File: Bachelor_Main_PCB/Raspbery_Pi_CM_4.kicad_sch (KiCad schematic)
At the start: 4 parts, among them J21 M20-9990245, U1 SC0683, X1 DF40HC_3.0_-100DS-0.4V_58, X2 DF40HC_3.0_-100DS-0.4V_58

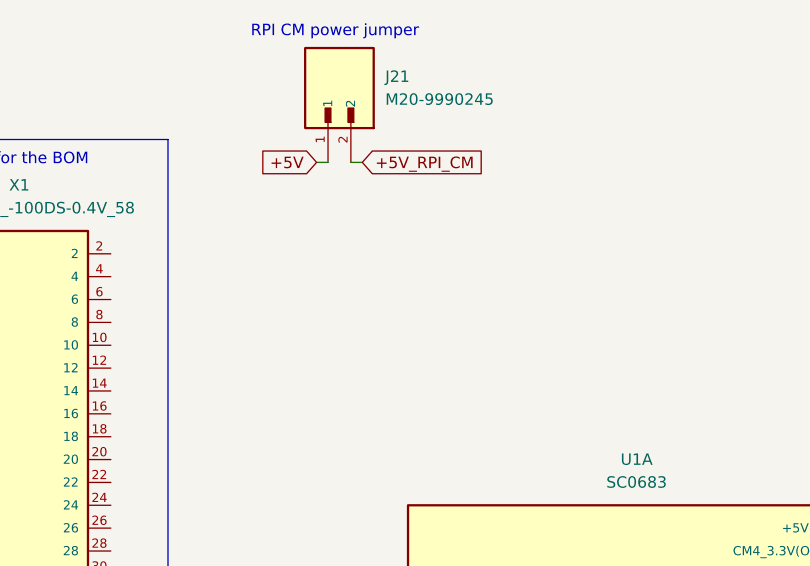
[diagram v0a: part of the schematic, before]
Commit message: Reinstated Mosfet RPI_CM_ENABLE controll
instead of enable pin on switch mode controller. this way the audiomoth can use the 5v supply with the capacitor multiplier.
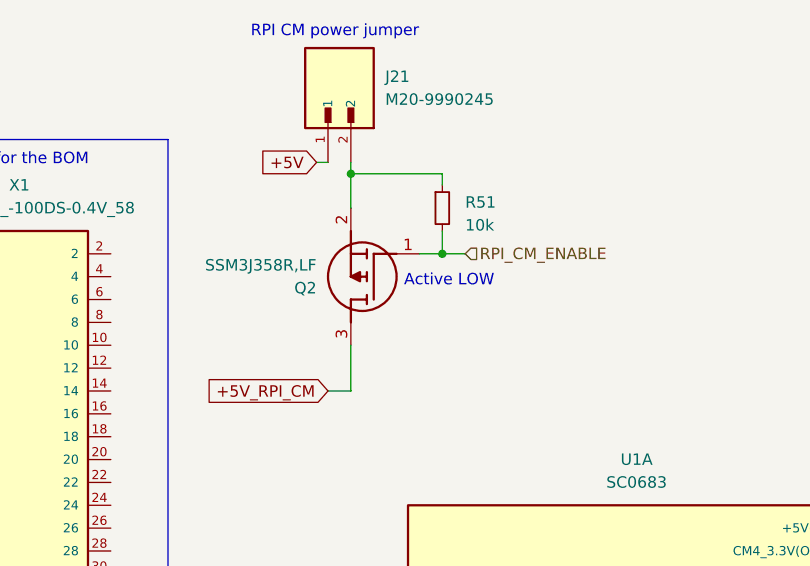
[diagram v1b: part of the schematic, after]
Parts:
- added Q2: SSM3J358R,LF, KiCad4:SOTFL95P240X88-3N, symbol SSM3J358R_LF:SSM3J358R,LF
- added R51: 10k, Resistor_SMD:R_0402_1005Metric, symbol Device:R_Small
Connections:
- net +5V_RPI_CM: now also Q2.3 (D); no longer J21.2
- new net: J21.2, Q2.2 (S), R51.1
- new net RPI_CM_ENABLE: Q2.1 (G), R51.2
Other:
- note added: "Active LOW"

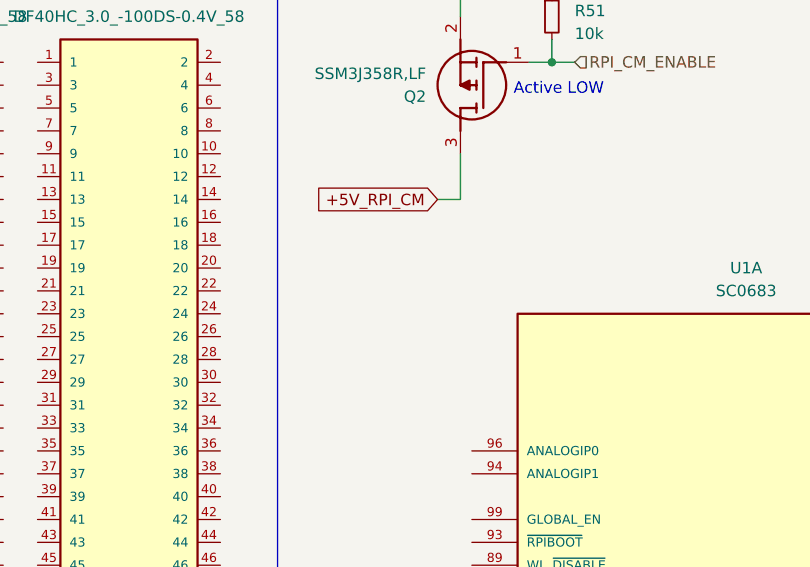
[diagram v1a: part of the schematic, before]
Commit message: Add green led to all power rails
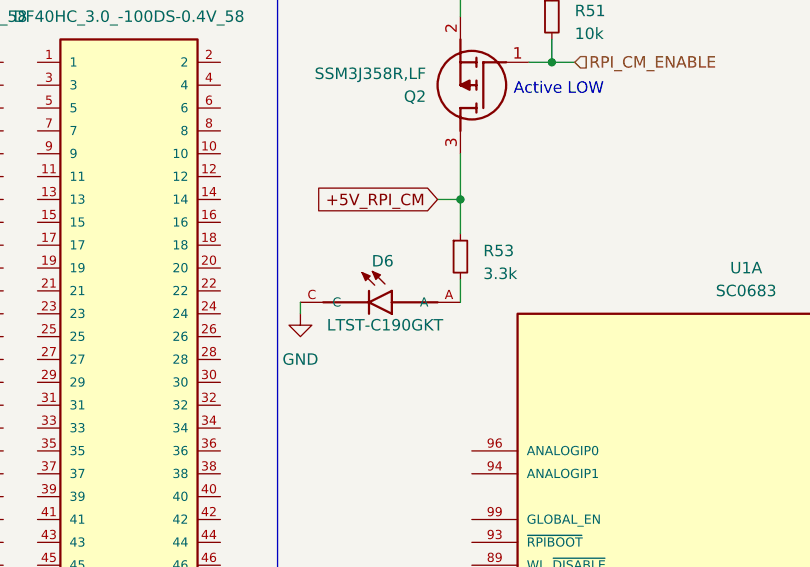
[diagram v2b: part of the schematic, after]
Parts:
- added D6: LTST-C190GKT, LTST-C190GKT:LEDM1608X80, symbol LTST-C190GKT:LTST-C190GKT
- added R53: 3.3k, Resistor_SMD:R_0402_1005Metric, symbol Device:R_Small
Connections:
- net +5V_RPI_CM: now also R53.1
- net GND: now also D6.C
- new net: D6.A, R53.2

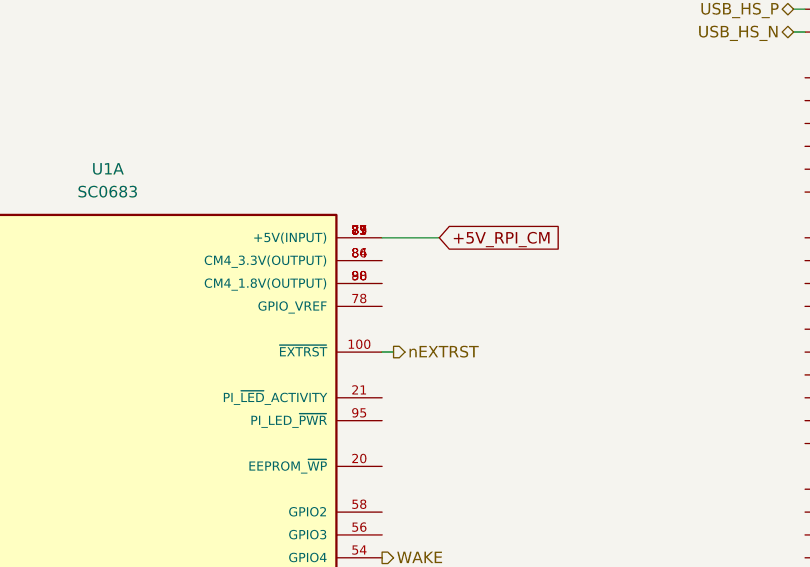
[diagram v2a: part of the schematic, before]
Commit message: connect RPI GPIO_VREF to internal 3,3v regulator
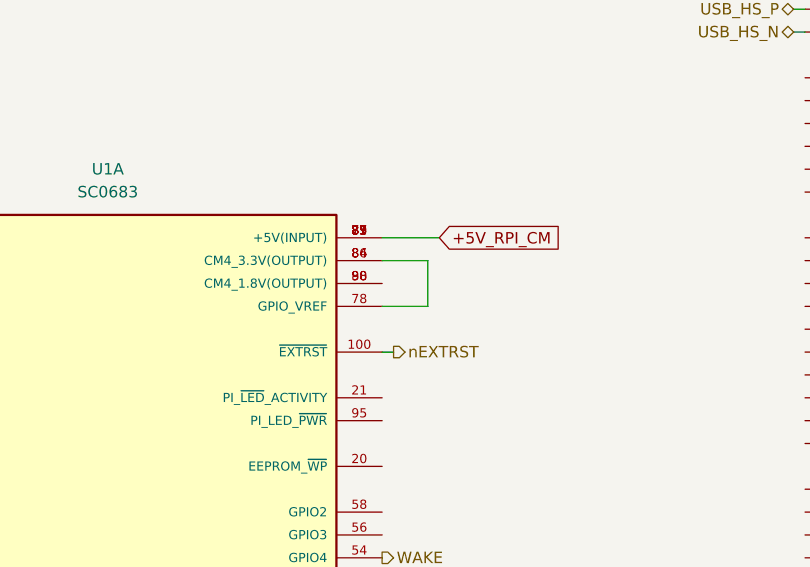
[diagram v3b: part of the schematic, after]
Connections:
- net at U1.78 (GPIO_VREF): now also U1.84 (CM4_3.3V(OUTPUT)), U1.86 (CM4_3.3V(OUTPUT))

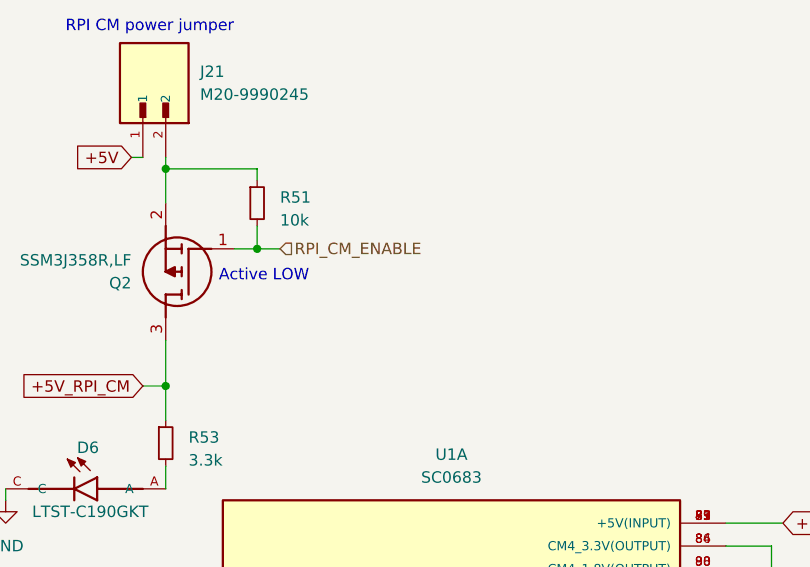
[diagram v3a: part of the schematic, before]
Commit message: Add signal inverter to RPIcm enable pin.
In order to protect MCU against 5v input on GPIO pin.
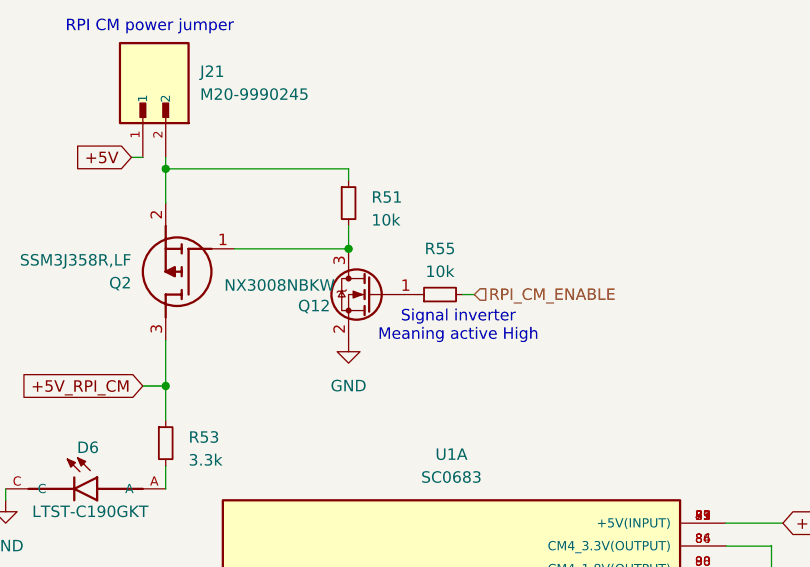
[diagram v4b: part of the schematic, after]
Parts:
- added Q12: NX3008NBKW, Package_TO_SOT_SMD:SOT-323_SC-70, symbol Device:Q_NMOS_GSD
- added R55: 10k, Resistor_SMD:R_0402_1005Metric, symbol Device:R_Small
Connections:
- net GND: now also Q12.2 (S)
- net RPI_CM_ENABLE: now also R55.2; no longer Q2.1 (G), R51.2
- new net: Q12.1 (G), R55.1
- new net: Q12.3 (D), Q2.1 (G), R51.2
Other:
- note added: "Signal inverter Meaning active High"
- note removed: "Active LOW"
- moved on the sheet: R51

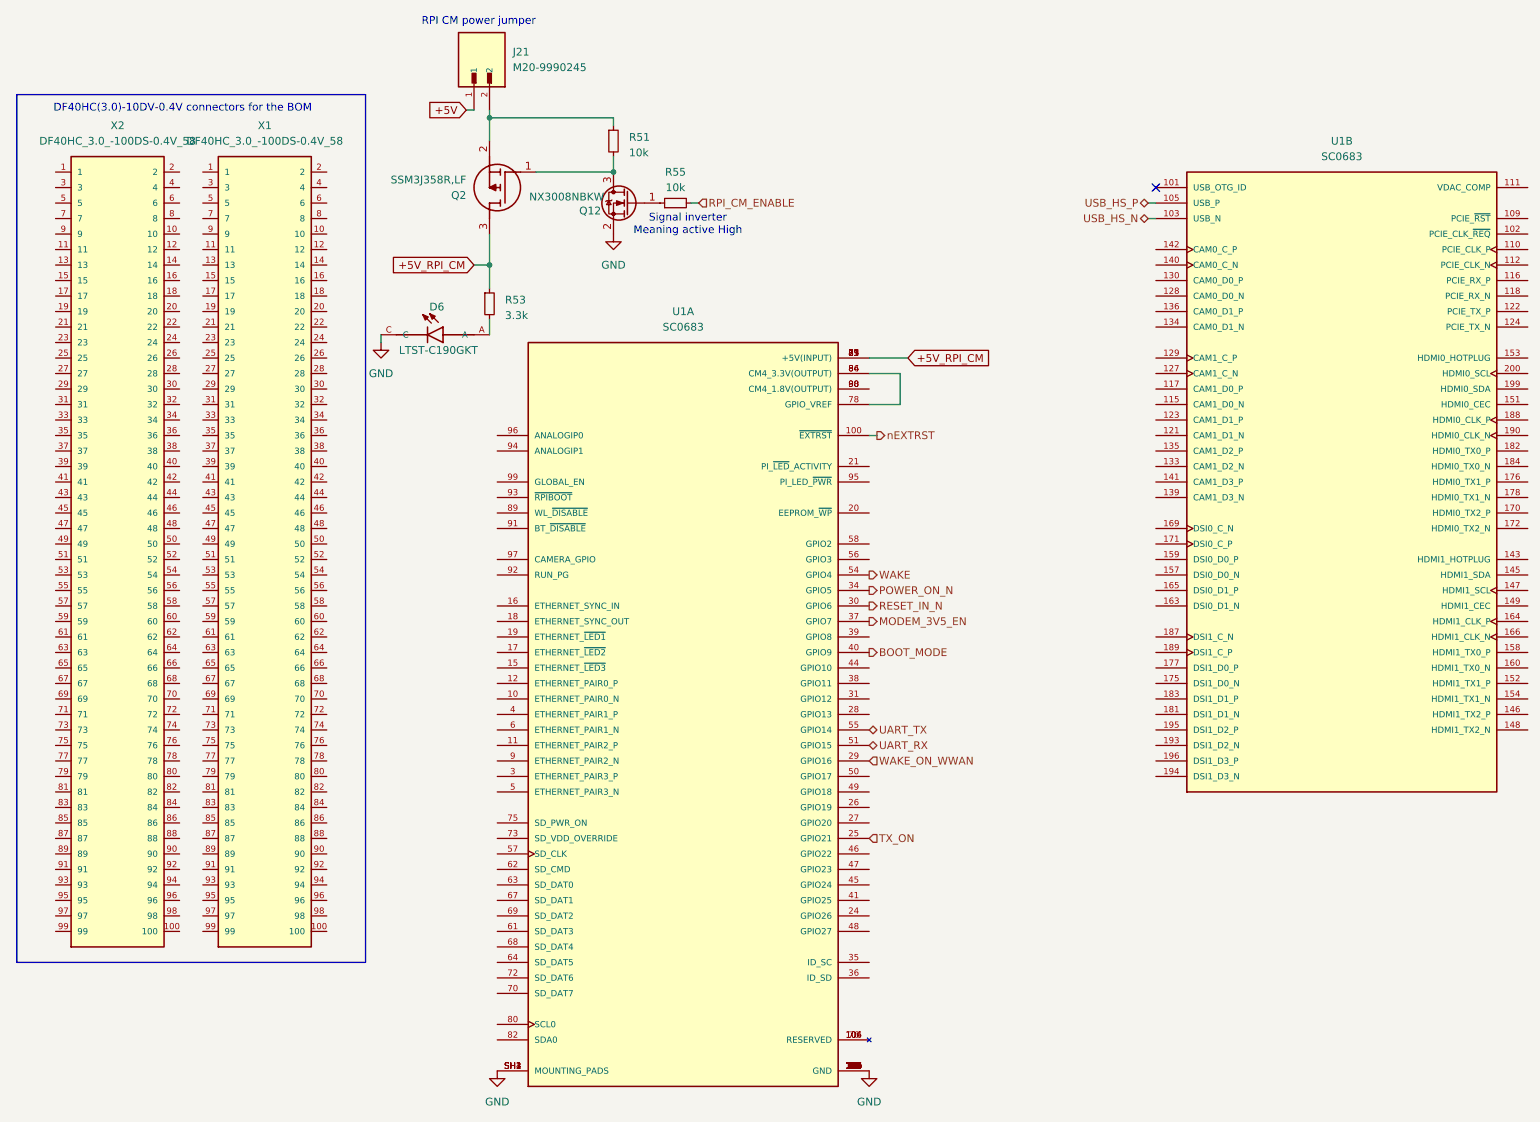
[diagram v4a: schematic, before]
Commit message: Updated the "Part-no" field in the symbol field table for all components
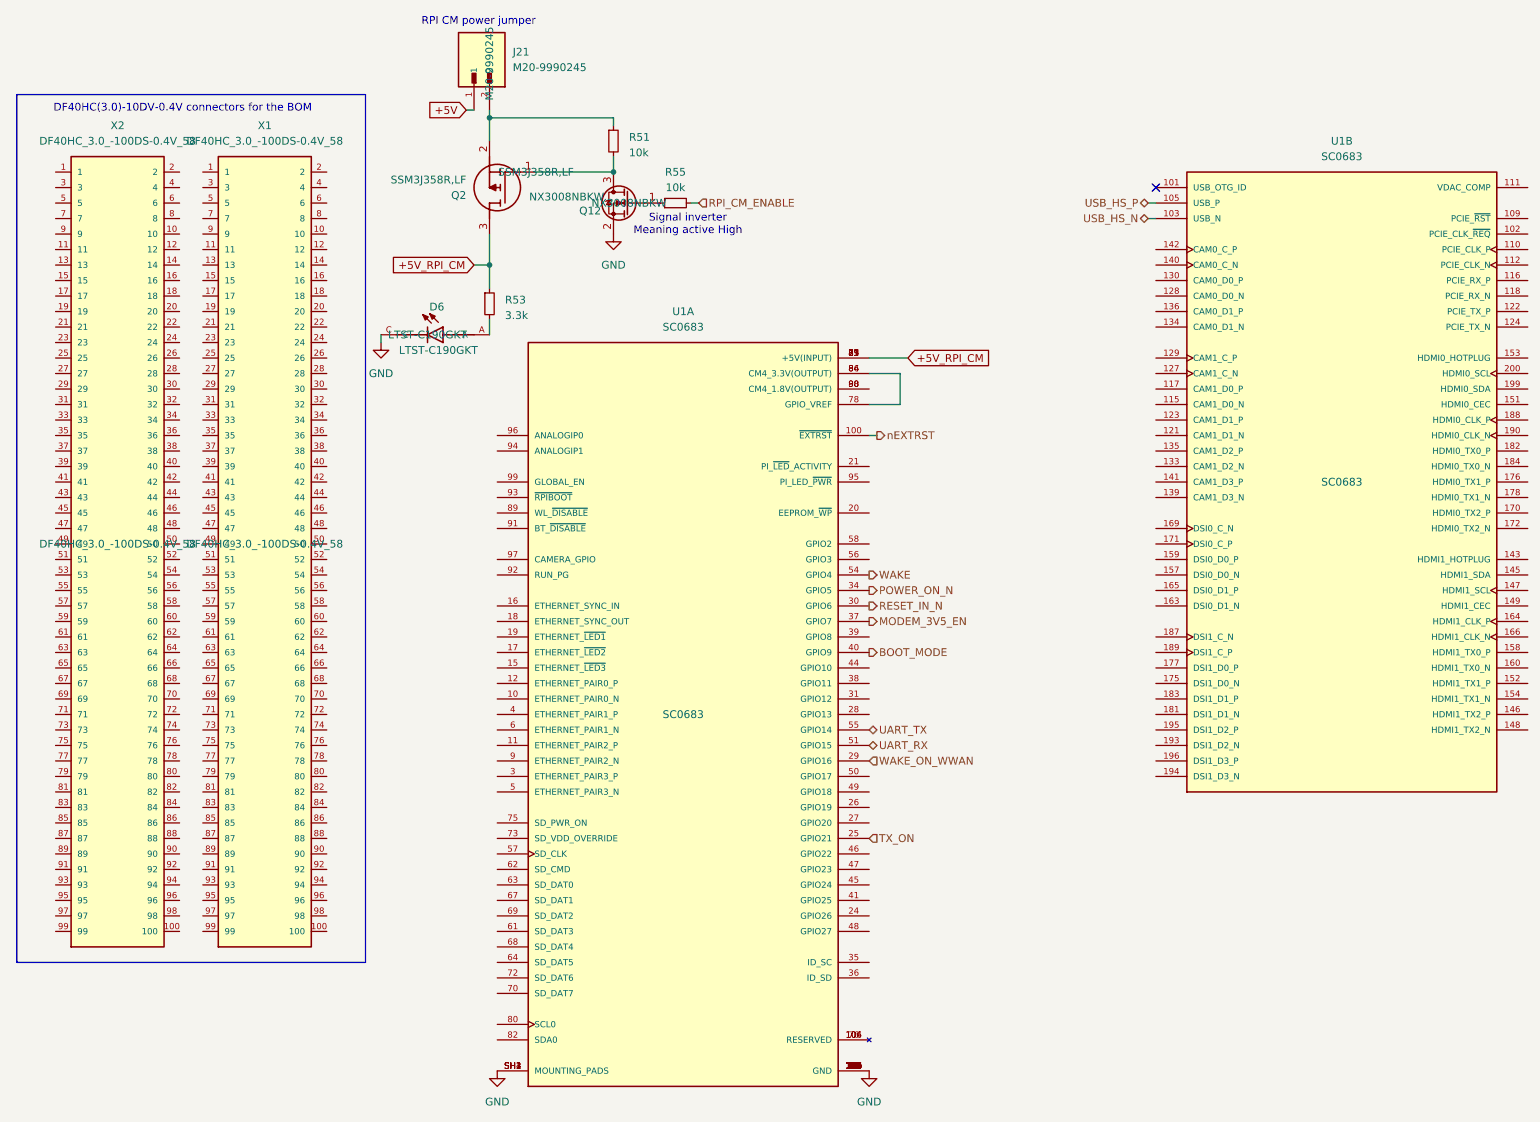
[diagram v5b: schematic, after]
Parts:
- D6: Part-no (none) -> LTST-C190GKT
- J21: Part-no (none) -> M20-9990245
- Q12: Part-no (none) -> NX3008NBKW
- Q2: Part-no (none) -> SSM3J358R,LF
- U1: Part-no (none) -> SC0683
- X1, X2: Part-no (none) -> DF40HC_3.0_-100DS-0.4V_58

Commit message: All resistors and capacitors correct footprints
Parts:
- R51, R53, R55: footprint Resistor_SMD:R_0402_1005Metric -> Resistor_SMD:R_0603_1608Metric
